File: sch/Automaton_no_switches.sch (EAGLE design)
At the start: 27 parts, among them IC1 74LS595D, IC2 74LS595D, IC3 74LS595D, IC4 74LS595D, IC5 74LS595D, J1 POWER_JACKPTH

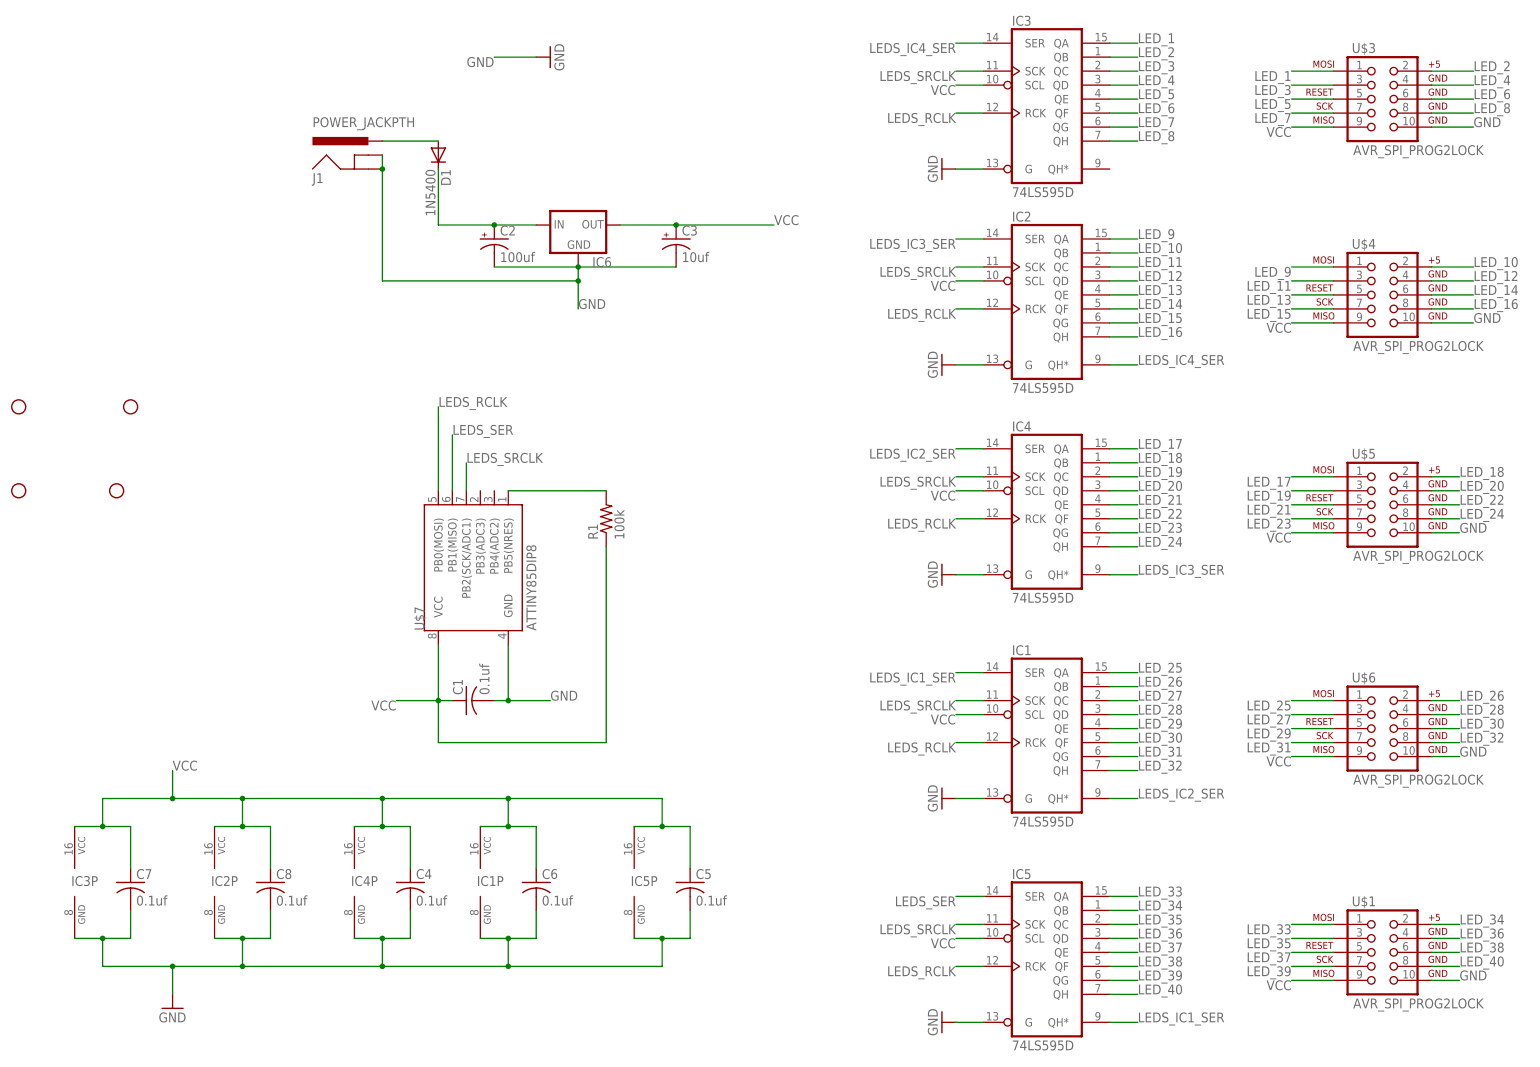
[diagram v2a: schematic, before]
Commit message: reduced the board size, added some parts to the schematic and board (power switch, breakout for unused MCU pins, power LED)
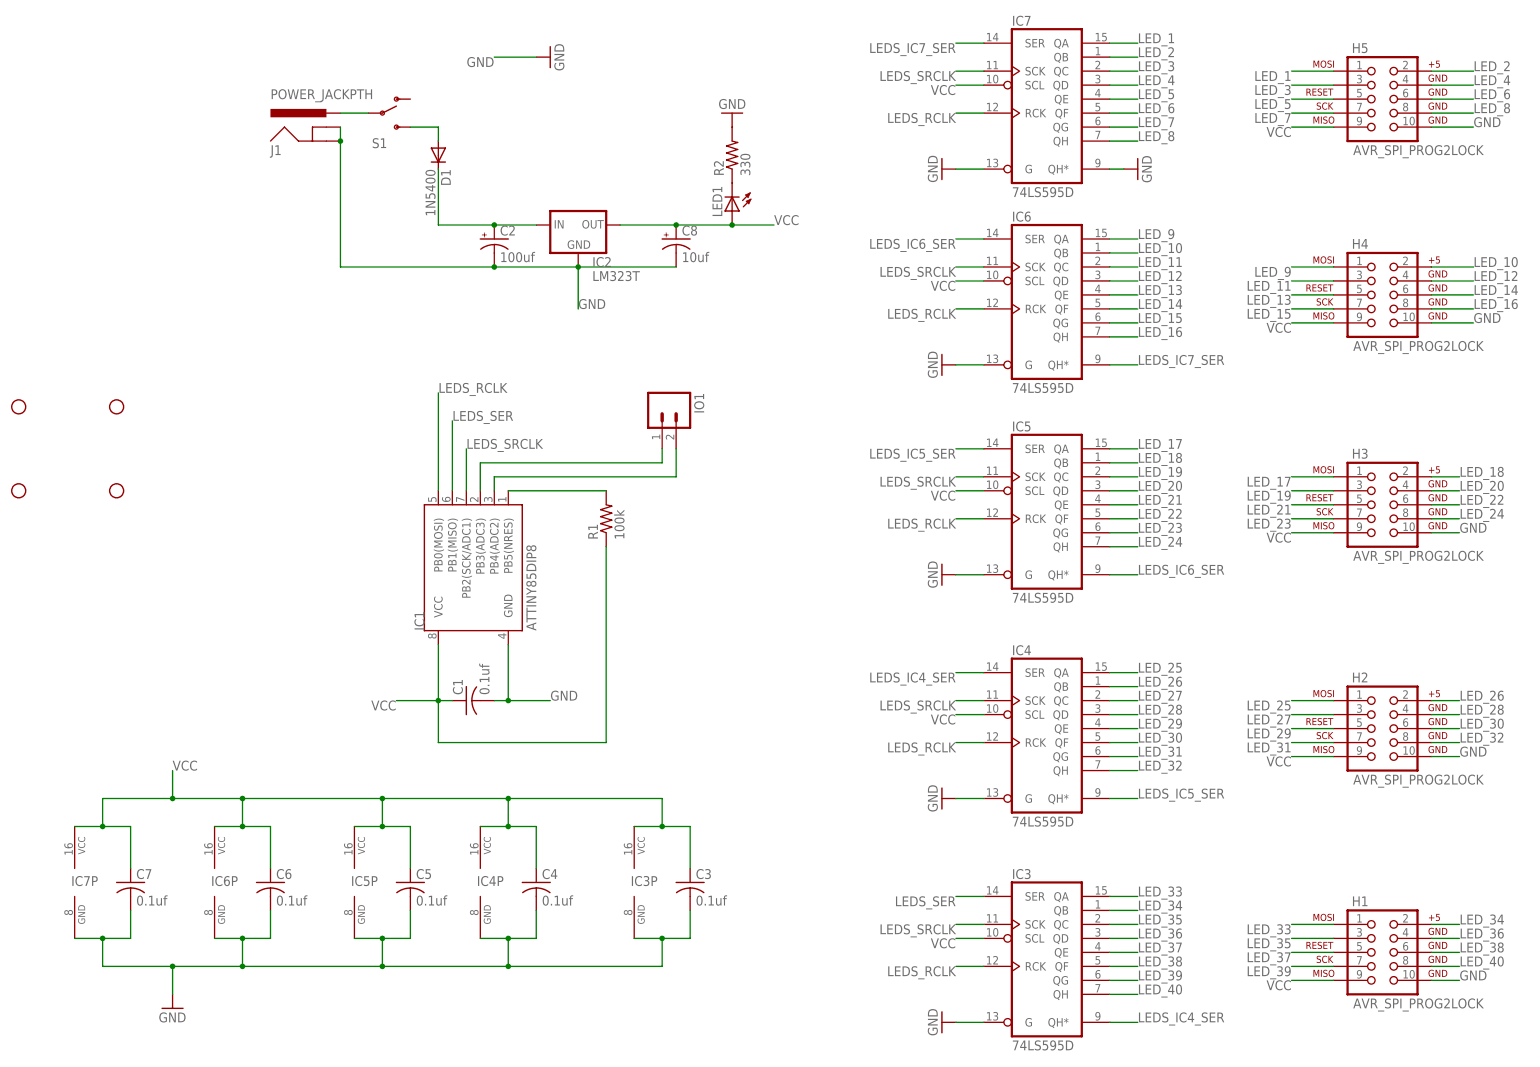
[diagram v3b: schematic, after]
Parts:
- removed JP2: STAND-OFF, SparkFun-Electromechanical:STAND-OFF
- removed U$7: ATTINY85DIP8, *Personal Library:ATTINY85DIP8
- added HOLE1: STAND-OFF, SparkFun-Electromechanical:STAND-OFF
- added IC7: 74LS595D, 74xx-us:74LS595D
- added IO1: (no value), SparkFun-Connectors:M02PTH3
- added LED1: (no value), led:LEDSMT1206
- added R2: 330, resistor:R-US_M1206
- added S1: (no value), SparkFun-Electromechanical:SWITCH-SPDTPTH_LOCK
- C3: value 10uf -> 0.1uf; device rcl:CPOL-USE2-5 -> resistor:C-USC1206
- C8: value 0.1uf -> 10uf; device resistor:C-USC1206 -> rcl:CPOL-USE2-5
- IC1: value 74LS595D -> ATTINY85DIP8; device 74xx-us:74LS595D -> *Personal Library:ATTINY85DIP8
- IC2: value 74LS595D -> LM323T; device 74xx-us:74LS595D -> SparkFun-PowerIC:V_REG_78XXSINK
- IC6: value (none) -> 74LS595D; device SparkFun-PowerIC:V_REG_78XXSINK -> 74xx-us:74LS595D
- renumbered JP1 to HOLE4, JP3 to HOLE3, JP4 to HOLE2, U$1 to H1, U$3 to H5, U$4 to H4, U$5 to H3, U$6 to H2
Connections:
- removed net LEDS_IC1_SER: IC1A.SER, IC5A.QH*
- removed net LEDS_IC2_SER: IC1A.QH*, IC4A.SER
- removed net LEDS_IC3_SER: IC2A.SER, IC4A.QH*
- new net LEDS_IC5_SER: IC4A.QH*, IC5A.SER
- new net LEDS_IC6_SER: IC5A.QH*, IC6A.SER
- new net LEDS_IC7_SER: IC6A.QH*, IC7A.SER
- new net N$4: D1.A, S1.S
- new net N$5: LED1.C, R2.1
- new net PB3: IC1.PB3(ADC3), IO1.1
- new net PB4: IC1.PB4(ADC2), IO1.2
- net GND: now also C3.2, C8.-, IC1.GND, IC2.GND, IC6A.G, IC6P.GND, IC7A.G, IC7A.QH*, IC7P.GND, R2.2; no longer C3.-, C8.2, IC1A.G, IC1P.GND, IC2A.G, IC2P.GND, IC6.GND, U$7.GND
- net LEDS_IC4_SER: now also IC3A.QH*, IC4A.SER; no longer IC2A.QH*, IC3A.SER
- net LEDS_RCLK: now also IC1.PB0(MOSI), IC6A.RCK, IC7A.RCK; no longer IC1A.RCK, IC2A.RCK, U$7.PB0(MOSI)
- net LEDS_SER: now also IC1.PB1(MISO), IC3A.SER; no longer IC5A.SER, U$7.PB1(MISO)
- net LEDS_SRCLK: now also IC1.PB2(SCK/ADC1), IC6A.SCK, IC7A.SCK; no longer IC1A.SCK, IC2A.SCK, U$7.PB2(SCK/ADC1)
- net LED_1: now also IC7A.QA; no longer IC3A.QA
- net LED_10: now also IC6A.QB; no longer IC2A.QB
- net LED_11: now also IC6A.QC; no longer IC2A.QC
- net LED_12: now also IC6A.QD; no longer IC2A.QD
- net LED_13: now also IC6A.QE; no longer IC2A.QE
- net LED_14: now also IC6A.QF; no longer IC2A.QF
- net LED_15: now also IC6A.QG; no longer IC2A.QG
- net LED_16: now also IC6A.QH; no longer IC2A.QH
- net LED_17: now also IC5A.QA; no longer IC4A.QA
- net LED_18: now also IC5A.QB; no longer IC4A.QB
- net LED_19: now also IC5A.QC; no longer IC4A.QC
- net LED_2: now also IC7A.QB; no longer IC3A.QB
- net LED_20: now also IC5A.QD; no longer IC4A.QD
- net LED_21: now also IC5A.QE; no longer IC4A.QE
- net LED_22: now also IC5A.QF; no longer IC4A.QF
- net LED_23: now also IC5A.QG; no longer IC4A.QG
- net LED_24: now also IC5A.QH; no longer IC4A.QH
- net LED_25: now also IC4A.QA; no longer IC1A.QA
- net LED_26: now also IC4A.QB; no longer IC1A.QB
- net LED_27: now also IC4A.QC; no longer IC1A.QC
- net LED_28: now also IC4A.QD; no longer IC1A.QD
- net LED_29: now also IC4A.QE; no longer IC1A.QE
- net LED_3: now also IC7A.QC; no longer IC3A.QC
- net LED_30: now also IC4A.QF; no longer IC1A.QF
- net LED_31: now also IC4A.QG; no longer IC1A.QG
- net LED_32: now also IC4A.QH; no longer IC1A.QH
- net LED_33: now also IC3A.QA; no longer IC5A.QA
- net LED_34: now also IC3A.QB; no longer IC5A.QB
- net LED_35: now also IC3A.QC; no longer IC5A.QC
- net LED_36: now also IC3A.QD; no longer IC5A.QD
- net LED_37: now also IC3A.QE; no longer IC5A.QE
- net LED_38: now also IC3A.QF; no longer IC5A.QF
- net LED_39: now also IC3A.QG; no longer IC5A.QG
- net LED_4: now also IC7A.QD; no longer IC3A.QD
- net LED_40: now also IC3A.QH; no longer IC5A.QH
- net LED_5: now also IC7A.QE; no longer IC3A.QE
- net LED_6: now also IC7A.QF; no longer IC3A.QF
- net LED_7: now also IC7A.QG; no longer IC3A.QG
- net LED_8: now also IC7A.QH; no longer IC3A.QH
- net LED_9: now also IC6A.QA; no longer IC2A.QA
- net N$1: now also IC2.IN; no longer IC6.IN
- net N$2: now also IC1.PB5(NRES); no longer U$7.PB5(NRES)
- net N$3: now also S1.P; no longer D1.A
- net VCC: now also C3.1, C8.+, IC1.VCC, IC2.OUT, IC6A.SCL, IC6P.VCC, IC7A.SCL, IC7P.VCC, LED1.A; no longer C3.+, C8.1, IC1A.SCL, IC1P.VCC, IC2A.SCL, IC2P.VCC, IC6.OUT, U$7.VCC
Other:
- moved on the sheet: C4, C5, C6, IC3, IC3P, IC4, IC4P, IC5, IC5P, J1
